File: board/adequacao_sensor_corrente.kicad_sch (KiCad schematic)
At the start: 10 parts, among them J8 Conn_01x03_Pin, U7 LM324

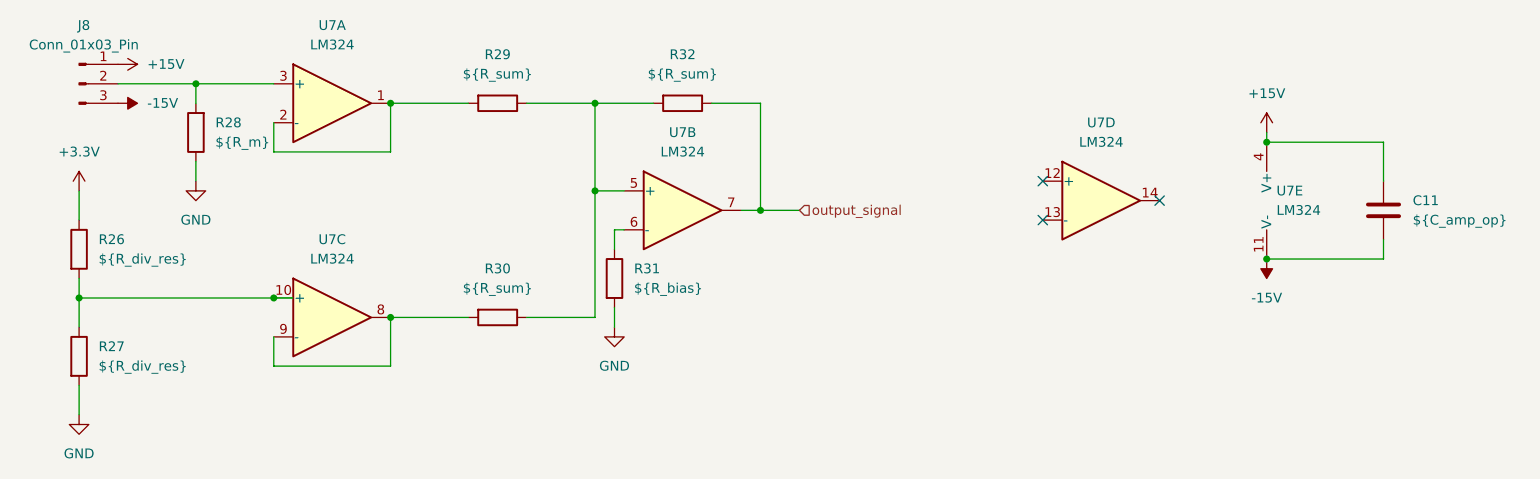
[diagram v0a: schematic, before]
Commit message: Finalização da placa, trilhas, planos de terra e footprint TJA1050
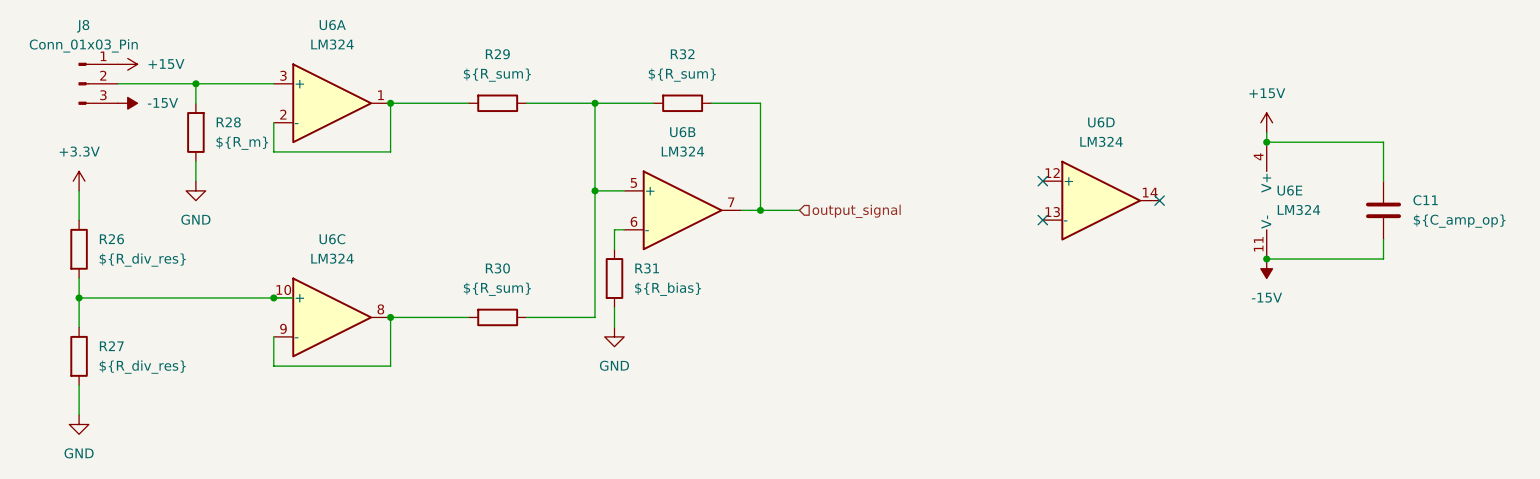
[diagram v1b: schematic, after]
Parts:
- renumbered U7 to U6

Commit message: Criação da placa de alimentação
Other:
- company: (none) -> Escola Politécnica da Universidade de São Paulo
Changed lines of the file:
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@@
 	(generator_version "8.0")
 	(paper "A4")
+	(title_block
+		(date "2025-10-02")
+		(company "Escola Politécnica da Universidade de São Paulo")
+	)
 	(junction
 		(at 92.71 68.58)
